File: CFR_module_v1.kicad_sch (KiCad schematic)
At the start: 66 parts, among them J1 Conn_01x20, J2 Conn_01x20, Q1 NPN

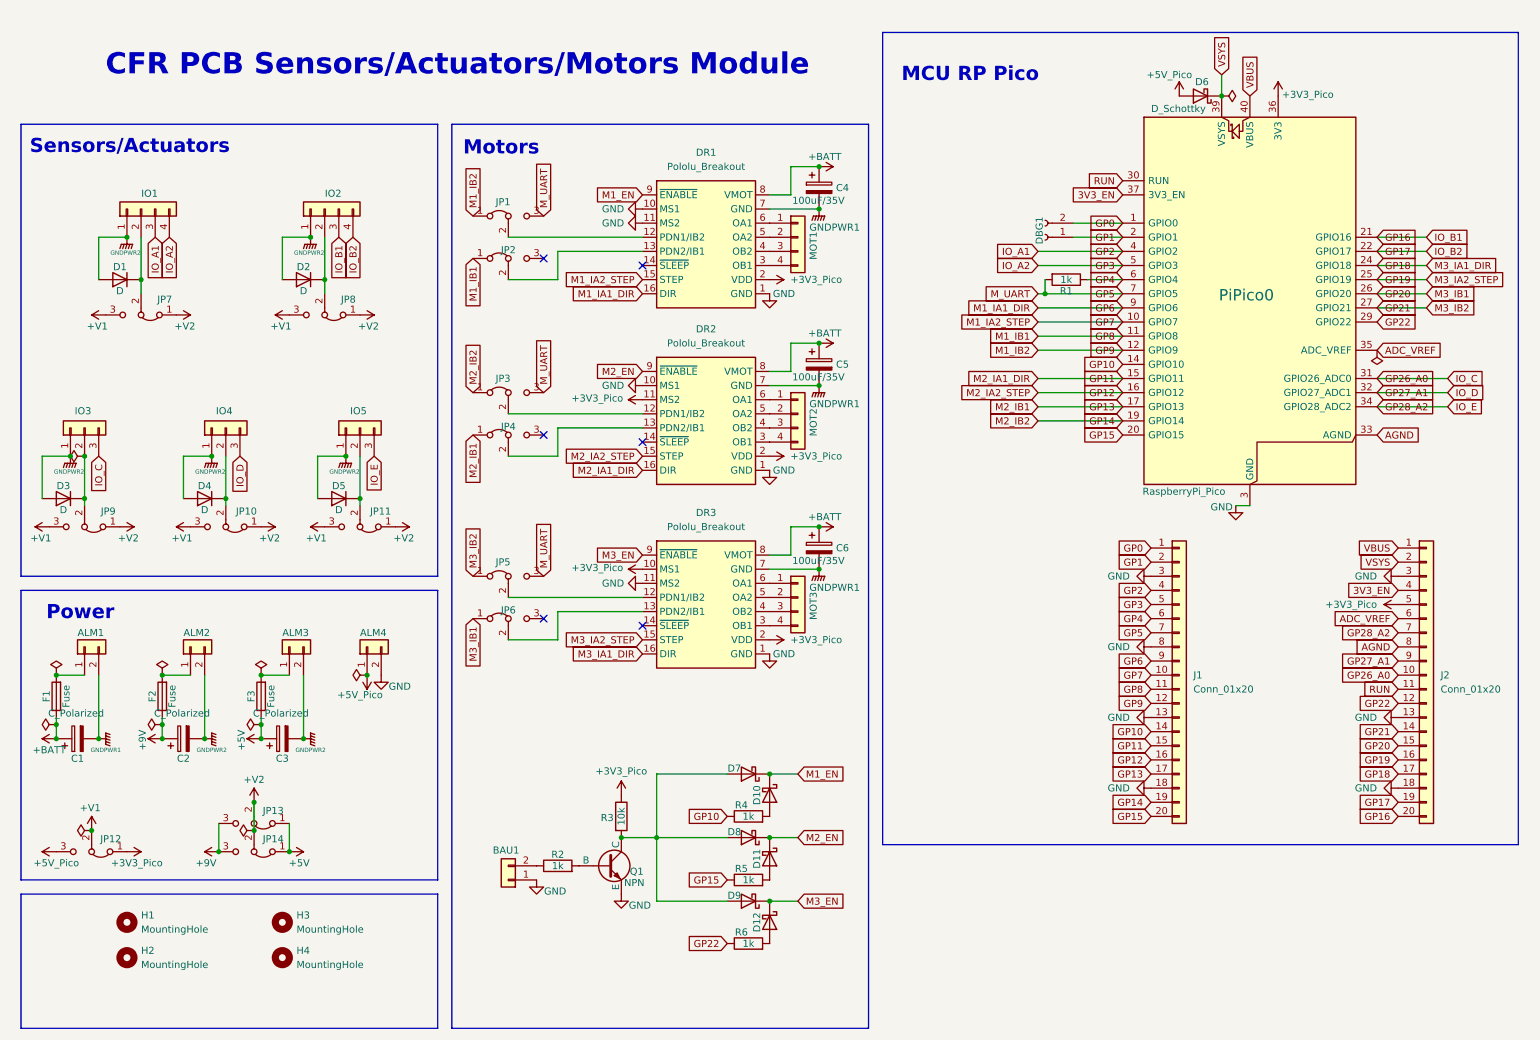
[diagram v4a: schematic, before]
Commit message: GND commun et ajout de branchements batterie
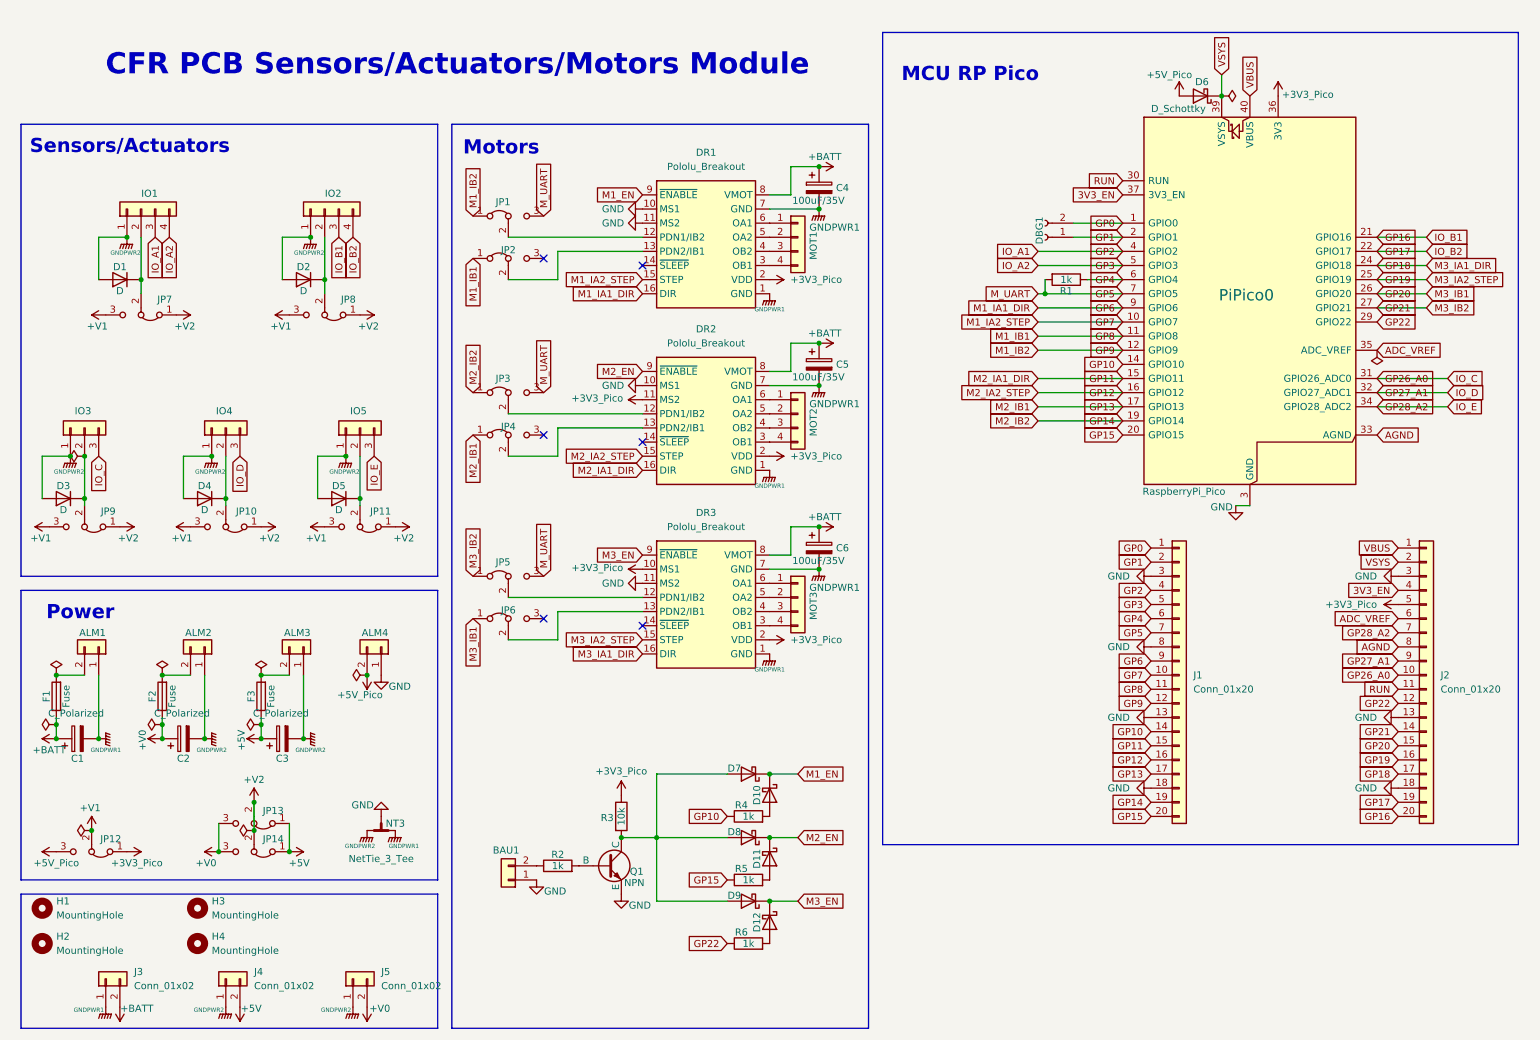
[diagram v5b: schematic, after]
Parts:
- added J3, J4, J5: Conn_01x02, Connector_PinHeader_2.54mm:PinHeader_1x02_P2.54mm_Vertical, symbol Connector_Generic:Conn_01x02
- added NT3: NetTie_3_Tee, NetTie:NetTie-3_SMD_Pad2.0mm, symbol Device:NetTie_3_Tee
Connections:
- net +5V: now also J4.2 (Pin_2)
- net +5V_Pico: now also ALM4.2 (Pin_2); no longer ALM4.1 (Pin_1)
- net +BATT: now also J3.2 (Pin_2)
- net GND: now also ALM4.1 (Pin_1), NT3.3; no longer ALM4.2 (Pin_2), DR1.1 (GND), DR2.1 (GND), DR3.1 (GND)
- net GNDPWR1: now also ALM1.1 (Pin_1), DR1.1 (GND), DR2.1 (GND), DR3.1 (GND), J3.1 (Pin_1), NT3.1; no longer ALM1.2 (Pin_2)
- net GNDPWR2: now also ALM2.1 (Pin_1), ALM3.1 (Pin_1), J4.1 (Pin_1), J5.1 (Pin_1), NT3.2; no longer ALM2.2 (Pin_2), ALM3.2 (Pin_2)
- net at F1.2: now also ALM1.2 (Pin_2); no longer ALM1.1 (Pin_1)
- net at F2.2: now also ALM2.2 (Pin_2); no longer ALM2.1 (Pin_1)
- net at F3.2: now also ALM3.2 (Pin_2); no longer ALM3.1 (Pin_1)
- net +9V renamed +V0
- net +V0: now also J5.2 (Pin_2)
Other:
- moved on the sheet: ALM1, ALM2, ALM3, ALM4, H1, H2, H3, H4

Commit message: ajout d'explication sur schematics
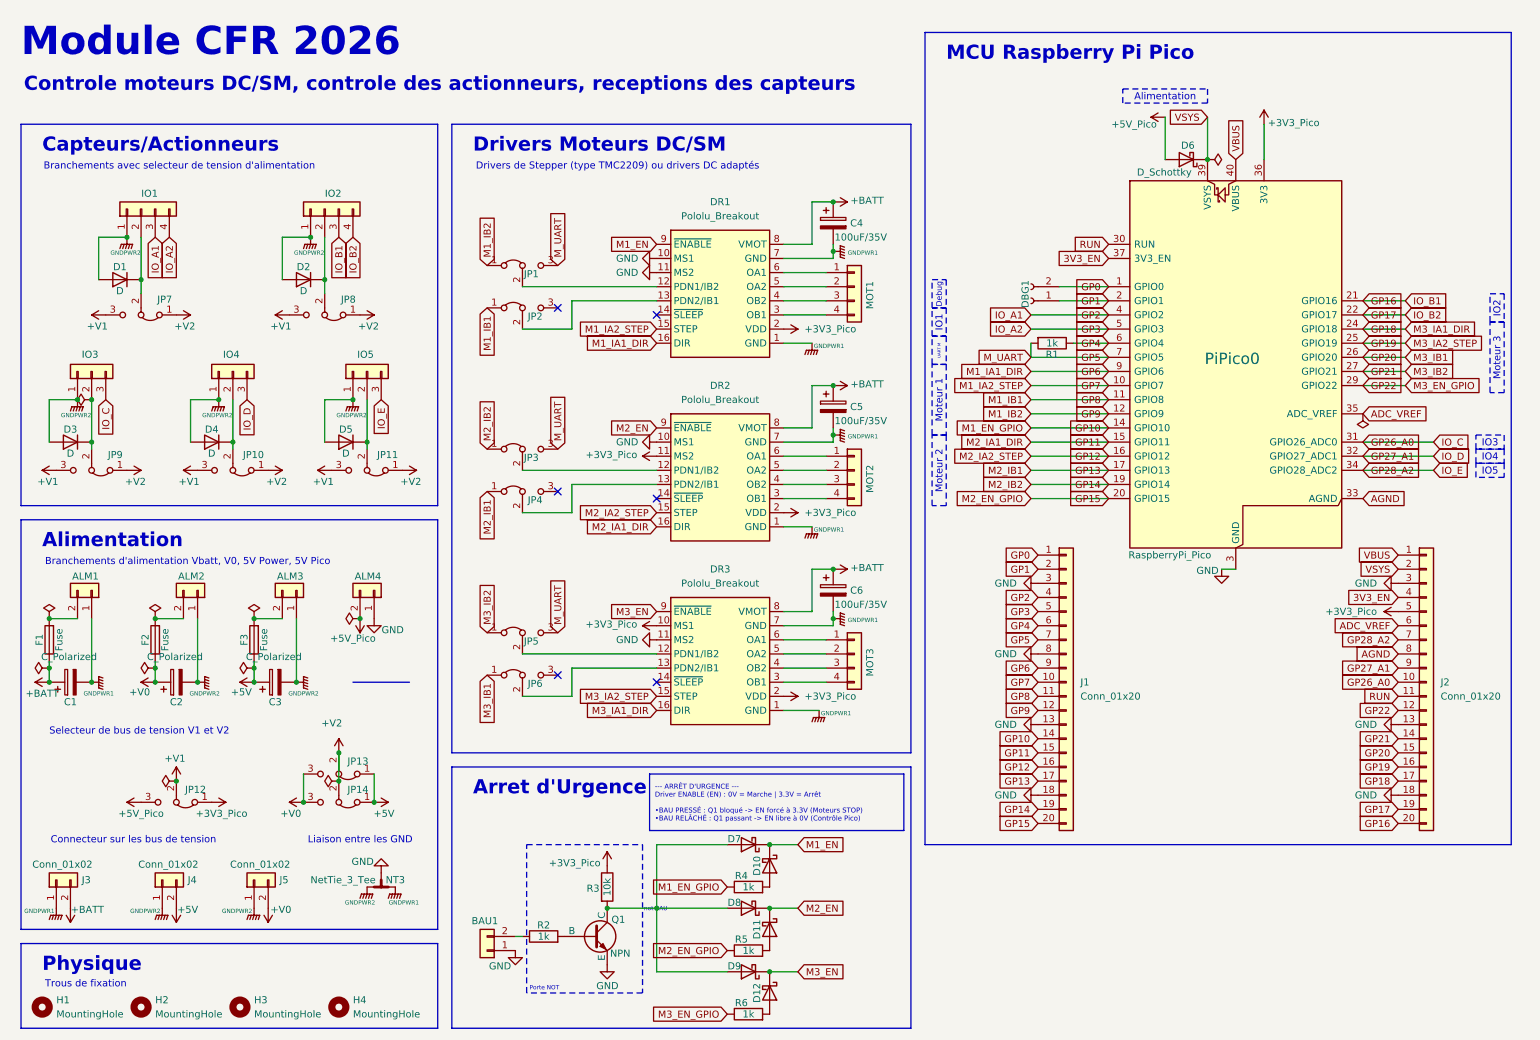
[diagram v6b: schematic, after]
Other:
- note added: "Alimentation"
- note added: "Arret d'Urgence"
- note added: "Branchements avec selecteur de tension d'alimentation"
- note added: "Branchements d'alimentation Vbatt, V0, 5V Power, 5V Pico"
- note added: "Capteurs/Actionneurs"
- note added: "Connecteur sur les bus de tension"
- note added: "Controle moteurs DC/SM, controle des actionneurs, receptions des capteurs"
- note added: "Drivers Moteurs DC/SM"
- note added: "Drivers de Stepper (type TMC2209) ou drivers DC adaptés"
- note added: "Liaison entre les GND"
- note added: "MCU Raspberry Pi Pico"
- note added: "Module CFR 2026"
- note added: "Physique"
- note added: "Porte NOT"
- note added: "Selecteur de bus de tension V1 et V2"
- note added: "Trous de fixation"
- note added: "not BAU"
- note removed: "CFR PCB Sensors/Actuators/Motors Module"
- note removed: "MCU RP Pico"
- note removed: "Motors"
- note removed: "Power"
- note removed: "Sensors/Actuators"
- company: (none) -> Pinguin Centrale Bot
- title: (none) -> Module Principal CFR 2026
- moved on the sheet: ALM1, ALM2, ALM3, ALM4, BAU1, C1, C2, C3, C4, D10, D11, D12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

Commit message: Placement composant front et silkscreen
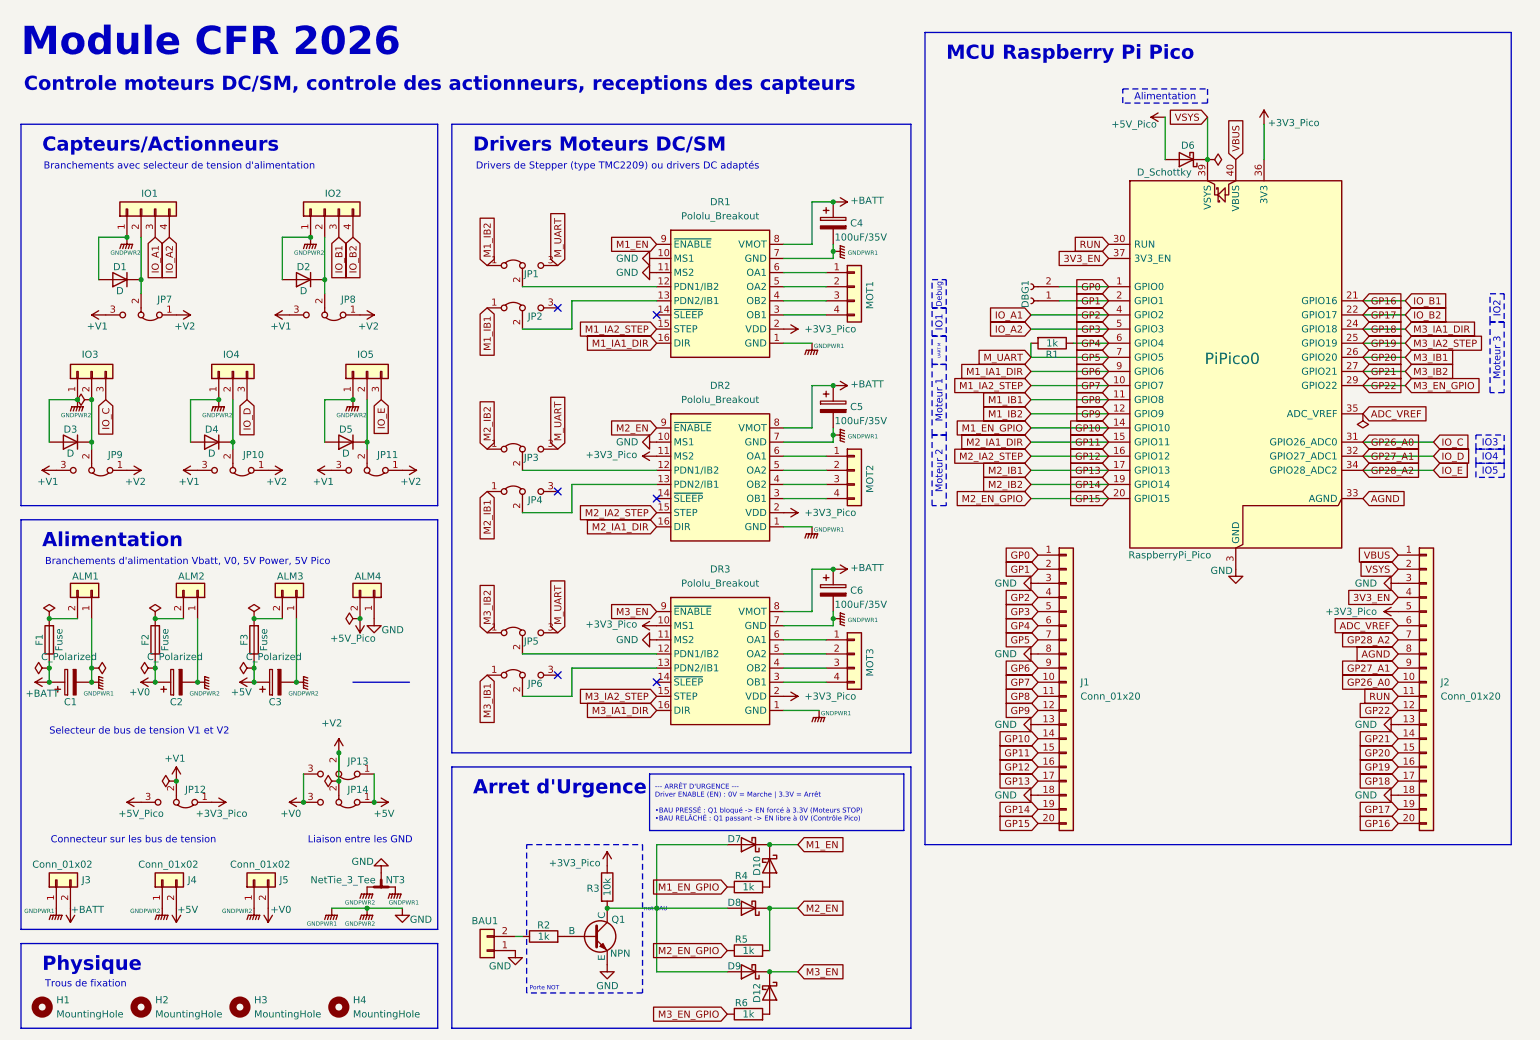
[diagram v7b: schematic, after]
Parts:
- removed D11: D_Schottky, Diode_SMD:D_SOD-123, symbol Device:D_Schottky
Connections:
- net GNDPWR1 is gone; now on net GND: ALM1.1 (Pin_1), C1.2, C4.2, C5.2, C6.2, DR1.1 (GND), DR1.7 (GND), DR2.1 (GND), DR2.7 (GND), DR3.1 (GND), DR3.7 (GND), J3.1 (Pin_1), NT3.1
- net GNDPWR2 is gone; now on net GND: ALM2.1 (Pin_1), ALM3.1 (Pin_1), C2.2, C3.2, D1.2 (A), D2.2 (A), D3.2 (A), D4.2 (A), D5.2 (A), IO1.1 (Pin_1), IO2.1 (Pin_1), IO3.1 (Pin_1), IO4.1 (Pin_1), IO5.1 (Pin_1), J4.1 (Pin_1), J5.1 (Pin_1), NT3.2
- net M2_EN: now also R5.2
